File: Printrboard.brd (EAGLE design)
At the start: 100.1 x 61 mm, 122 parts, among them J1 MICROSD, J3 ATX, Q1 RFP30N06LE, Q2 RFP30N06LE, Q3 RFP30N06LE, U1 LM2841, U2 A4982, U3 A4982, U4 A4982, U5 A4982, U6 AT90USB1286, U7 AP7313, U8 TXB0104, X1 16MHz, X2 USB-MICROB

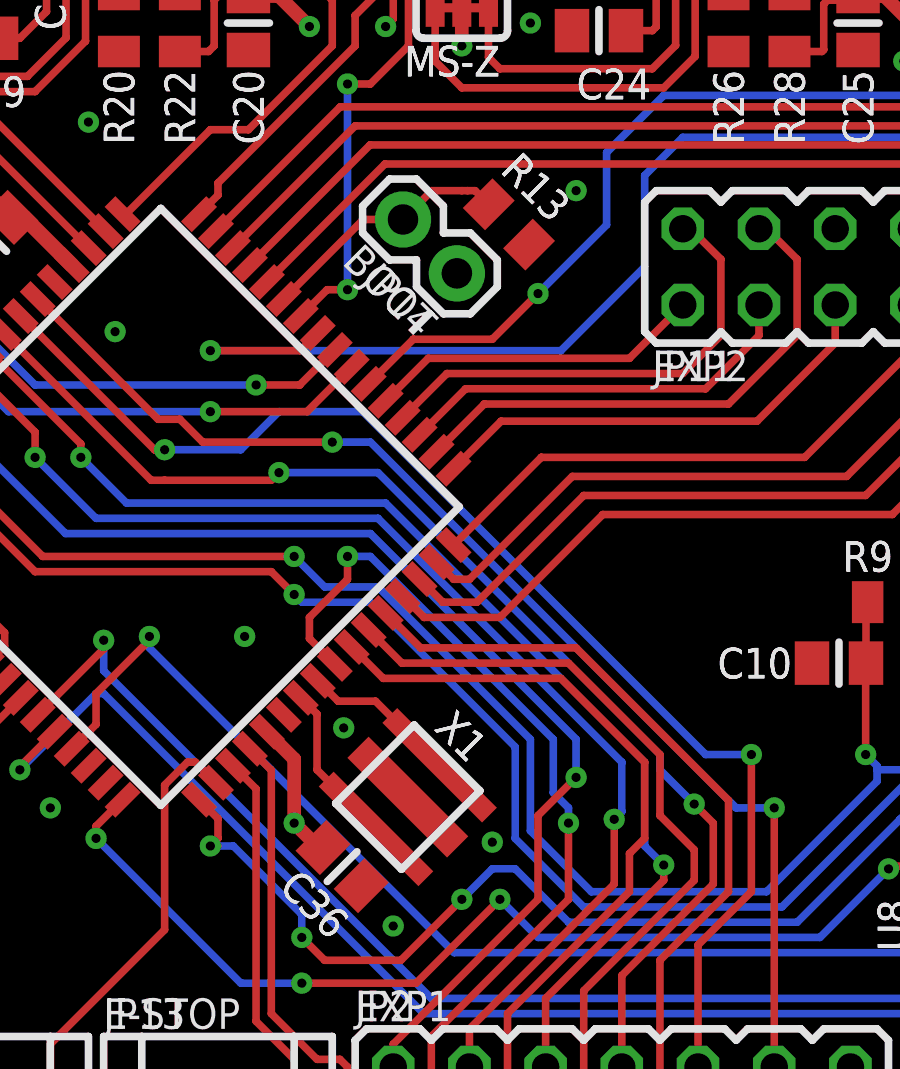
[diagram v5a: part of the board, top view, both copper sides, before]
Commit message: Make resonator pad larger to accomodate both available pacakages, and change polarity of BOOT jumper
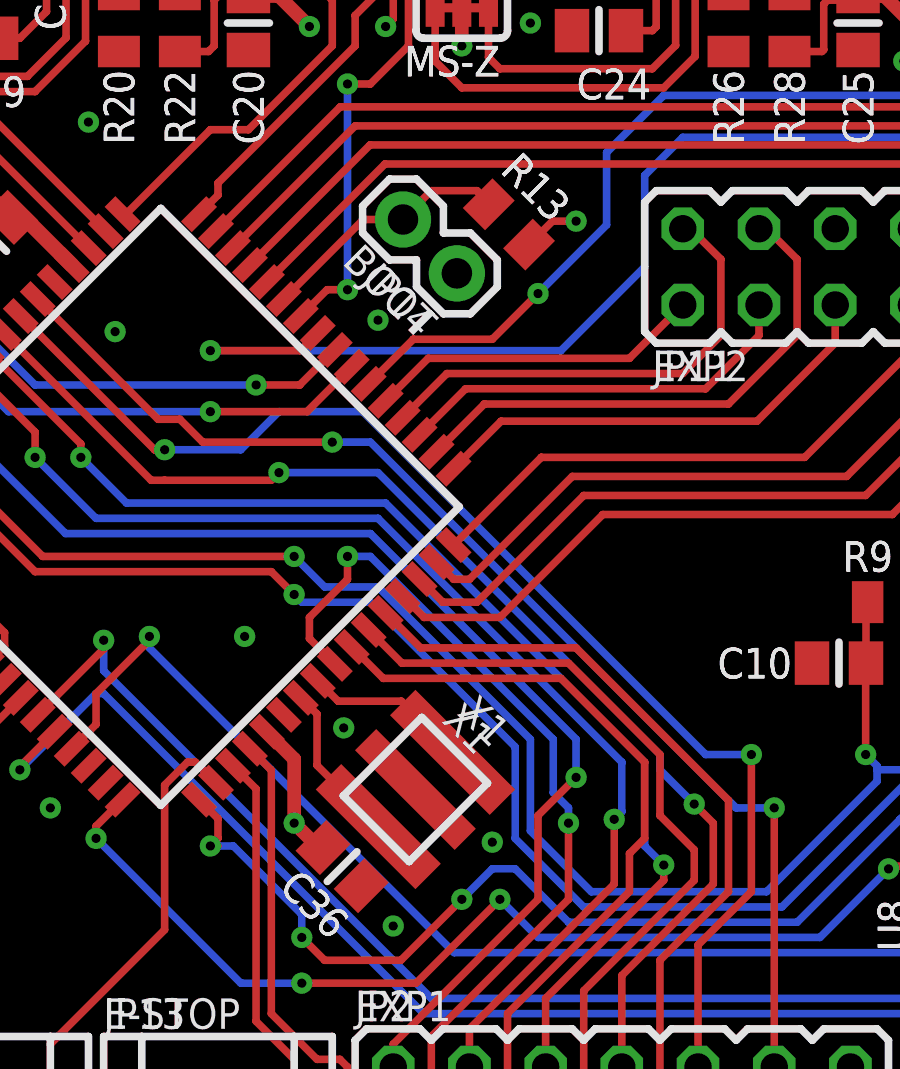
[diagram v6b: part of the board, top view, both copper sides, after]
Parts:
- JP14: value ALE -> BOOT
- moved X1 0.36 mm to (52.6, 14.1)
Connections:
- net +5V: now also R13.2; no longer JP14.1
- net GND: now also JP14.1; no longer R13.2
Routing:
- net +5V: track 151.9 -> 153.7 mm, vias 22 -> 23
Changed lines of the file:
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@@
 <layers>
 <layer number="1" name="Top" color="4" fill="1" visible="yes" active="yes"/>
-<layer number="2" name="PWR" color="16" fill="1" visible="yes" active="yes"/>
-<layer number="3" name="GND" color="17" fill="1" visible="yes" active="yes"/>
+<layer number="2" name="PWR" color="16" fill="1" visible="no" active="yes"/>
+<layer number="3" name="GND" color="17" fill="1" visible="no" active="yes"/>
 <layer number="4" name="Route4" color="1" fill="4" visible="no" active="no"/>
 <layer number="5" name="Route5" color="4" fill="4" visible="no" active="no"/>
@@
 <wire x1="26.199996875" y1="18.050003125" x2="24.600003125" y2="18.050003125" width="0.254" layer="121"/>
 <text x="24.892" y="17.926" size="1.016" layer="121" ratio="25" rot="R270">USBPWR</text>
-<wire x1="54.70636875" y1="14.033321875" x2="52.090065625" y2="11.417046875" width="0.254" layer="121"/>
-<wire x1="52.090065625" y1="11.417046875" x2="49.898046875" y2="13.609065625" width="0.254" layer="121"/>
-<wire x1="49.898046875" y1="13.609065625" x2="52.514321875" y2="16.22536875" width="0.254" layer="121"/>
-<wire x1="52.514321875" y1="16.22536875" x2="54.70636875" y2="14.033321875" width="0.254" layer="121"/>
-<text x="53.1479" y="16.086709375" size="1.016" layer="121" ratio="25" rot="R315">X1</text>
+<wire x1="54.96036875" y1="14.287321875" x2="52.344065625" y2="11.671046875" width="0.254" layer="121"/>
+<wire x1="52.344065625" y1="11.671046875" x2="50.152046875" y2="13.863065625" width="0.254" layer="121"/>
+<wire x1="50.152046875" y1="13.863065625" x2="52.768321875" y2="16.47936875" width="0.254" layer="121"/>
+<wire x1="52.768321875" y1="16.47936875" x2="54.96036875" y2="14.287321875" width="0.254" layer="121"/>
+<text x="53.9099" y="16.594709375" size="1.016" layer="121" ratio="25" rot="R315">X1</text>
 <wire x1="9.04600625" y1="2.774009375" x2="9.04600625" y2="4.37400625" width="0.254" layer="121"/>
 <wire x1="9.04600625" y1="4.37400625" x2="10.246003125" y2="4.37400625" width="0.254" layer="121"/>
@@
 <attribute name="VALUE" x="100.711" y="35.814" size="1.27" layer="27" rot="R90"/>
 </element>
-<element name="JP14" library="SparkFun" package="1X02" value="ALE" x="53.9379" y="31.2792" smashed="yes" rot="R135">
+<element name="JP14" library="SparkFun" package="1X02" value="BOOT" x="53.9379" y="31.2792" smashed="yes" rot="R135">
 <attribute name="NAME" x="53.3426" y="29.7961" size="1.016" layer="25" ratio="20" rot="R135"/>
 <attribute name="VALUE" x="57.0809" y="32.6262" size="1.27" layer="27" rot="R135"/>
@@
 <attribute name="VALUE" x="80.01" y="34.036" size="1.27" layer="27" rot="R270"/>
 </element>
-<element name="X1" library="printrbot" package="AWSCR" value="16MHz" x="52.3022" y="13.8212" smashed="yes" rot="R225">
-<attribute name="NAME" x="53.1479" y="16.0867" size="1.016" layer="25" ratio="20" rot="R315"/>
-<attribute name="VALUE" x="47.9888" y="13.4676" size="1.27" layer="27" rot="R315"/>
+<element name="X1" library="printrbot" package="AWSCR" value="16MHz" x="52.5562" y="14.0752" smashed="yes" rot="R225">
+<attribute name="NAME" x="53.4019" y="16.3407" size="1.016" layer="25" ratio="20" rot="R315"/>
+<attribute name="VALUE" x="48.2428" y="13.7216" size="1.27" layer="27" rot="R315"/>
 </element>
 <element name="C6" library="rcl" package="PANASONIC_D" value="100uF" x="10.922" y="54.102" smashed="yes" rot="R270">
@@
 <contactref element="JP12" pad="3"/>
 <contactref element="C13" pad="1"/>
-<contactref element="R13" pad="2"/>
 <contactref element="JP13" pad="3"/>
 <contactref element="C10" pad="1"/>
@@
 <contactref element="JP11" pad="1"/>
 <contactref element="JP4" pad="1"/>
-<via x="57.912" y="34.036" extent="1-16" drill="0.3048"/>
+<via x="51.308" y="29.718" extent="1-16" drill="0.3048"/>
 <via x="35.306" y="17.018" extent="1-16" drill="0.3048"/>
 <via x="32.893" y="32.385" extent="1-16" drill="0.3048"/>
@@
 <contactref element="X2" pad="MT5"/>
 <contactref element="X2" pad="MT6"/>
+<contactref element="JP14" pad="1"/>
 </signal>
 <signal name="!RESET">
@@
 <wire x1="48.17021875" y1="30.42464375" x2="50.820825" y2="33.07525" width="0.254" layer="1"/>
 <wire x1="50.820825" y1="33.07525" x2="52.141846875" y2="33.07525" width="0.254" layer="1"/>
-<wire x1="54.2924" y1="34.036" x2="54.102" y2="34.036" width="0.254" layer="1"/>
-<wire x1="54.102" y1="34.036" x2="53.086" y2="34.036" width="0.254" layer="1"/>
-<wire x1="52.141846875" y1="33.07525" x2="53.086" y2="34.019403125" width="0.254" layer="1"/>
-<wire x1="53.086" y1="34.019403125" x2="53.086" y2="34.036" width="0.254" layer="1"/>
-<wire x1="55.000346875" y1="33.58215" x2="54.546496875" y2="34.036" width="0.254" layer="1"/>
-<wire x1="54.546496875" y1="34.036" x2="54.2924" y2="34.036" width="0.254" layer="1"/>
+<wire x1="52.141846875" y1="33.07525" x2="52.141846875" y2="33.091846875" width="0.254" layer="1"/>
+<wire x1="52.141846875" y1="33.091846875" x2="53.086" y2="34.036" width="0.254" layer="1"/>
+<wire x1="53.086" y1="34.036" x2="54.61" y2="34.036" width="0.254" layer="1"/>
+<wire x1="54.61" y1="34.036" x2="55.118" y2="33.528" width="0.254" layer="1"/>
+<wire x1="55.118" y1="33.528" x2="55.000346875" y2="33.58215" width="0" layer="19" extent="1-1"/>
 </signal>
 <signal name="XTAL1">
 <contactref element="U6" pad="24"/>
 <contactref element="X1" pad="IN"/>
-<wire x1="49.9802" y1="17.018" x2="51.2266" y2="17.018" width="0.254" layer="1"/>
-<wire x1="53.362859375" y1="14.881859375" x2="53.362740625" y2="14.881859375" width="0.254" layer="1"/>
-<wire x1="53.362740625" y1="14.881859375" x2="51.2266" y2="17.018" width="0.254" layer="1"/>
-<wire x1="49.3015875" y1="17.696721875" x2="49.9802" y2="17.018109375" width="0.254" layer="1"/>
-<wire x1="49.9802" y1="17.018109375" x2="49.9802" y2="17.018" width="0.254" layer="1"/>
+<wire x1="53.793634375" y1="15.312634375" x2="52.08826875" y2="17.018" width="0.254" layer="1"/>
+<wire x1="52.08826875" y1="17.018" x2="49.980309375" y2="17.018" width="0.254" layer="1"/>
+<wire x1="49.3015875" y1="17.696721875" x2="49.980309375" y2="17.018" width="0.254" layer="1"/>
 </signal>
 <signal name="XTAL2">
 <contactref element="U6" pad="23"/>
 <contactref element="X1" pad="OUT"/>
-<wire x1="49.276" y1="14.732" x2="49.276" y2="16.590940625" width="0.254" layer="1"/>
-<wire x1="51.2415375" y1="12.7605375" x2="51.2415375" y2="12.7664625" width="0.254" layer="1"/>
-<wire x1="51.2415375" y1="12.7664625" x2="49.276" y2="14.732" width="0.254" layer="1"/>
 <wire x1="48.735903125" y1="17.1310375" x2="49.276" y2="16.590940625" width="0.254" layer="1"/>
+<wire x1="49.276" y1="16.590940625" x2="49.276" y2="14.880525" width="0.254" layer="1"/>
+<wire x1="51.3187625" y1="12.8377625" x2="49.276" y2="14.880525" width="0.254" layer="1"/>
 </signal>
 <signal name="PC2">
@@
 <contactref element="L1" pad="P$2"/>
 <contactref element="R12" pad="2"/>
-<contactref element="JP14" pad="1"/>
 <contactref element="R9" pad="2"/>
 <contactref element="R10" pad="2"/>
@@
 <contactref element="JP11" pad="2"/>
 <contactref element="JP4" pad="5"/>
-<wire x1="53.9379" y1="31.2792" x2="53.848" y2="31.2792" width="0.254" layer="16"/>
 <wire x1="23.84" y1="41.946" x2="23.84" y2="43.382" width="0.4572" layer="1"/>
 <wire x1="24.13" y1="41.656" x2="23.84" y2="41.946" width="0.4572" layer="1"/>
@@
 <wire x1="24.95" y1="20.516" x2="24.892" y2="20.574" width="0.3048" layer="1"/>
 <via x="24.892" y="20.574" extent="1-16" drill="0.3048"/>
+<contactref element="R13" pad="2"/>
+<wire x1="56.34385" y1="32.238646875" x2="57.125203125" y2="33.02" width="0.254" layer="1"/>
+<wire x1="57.125203125" y1="33.02" x2="57.912" y2="33.02" width="0.254" layer="1"/>
+<via x="57.912" y="33.02" extent="1-16" drill="0.3048"/>
 </signal>
 <signal name="SDDO">
@@
 </signal>
 </signals>
+<errors>
+</errors>
 </board>
 </drawing>

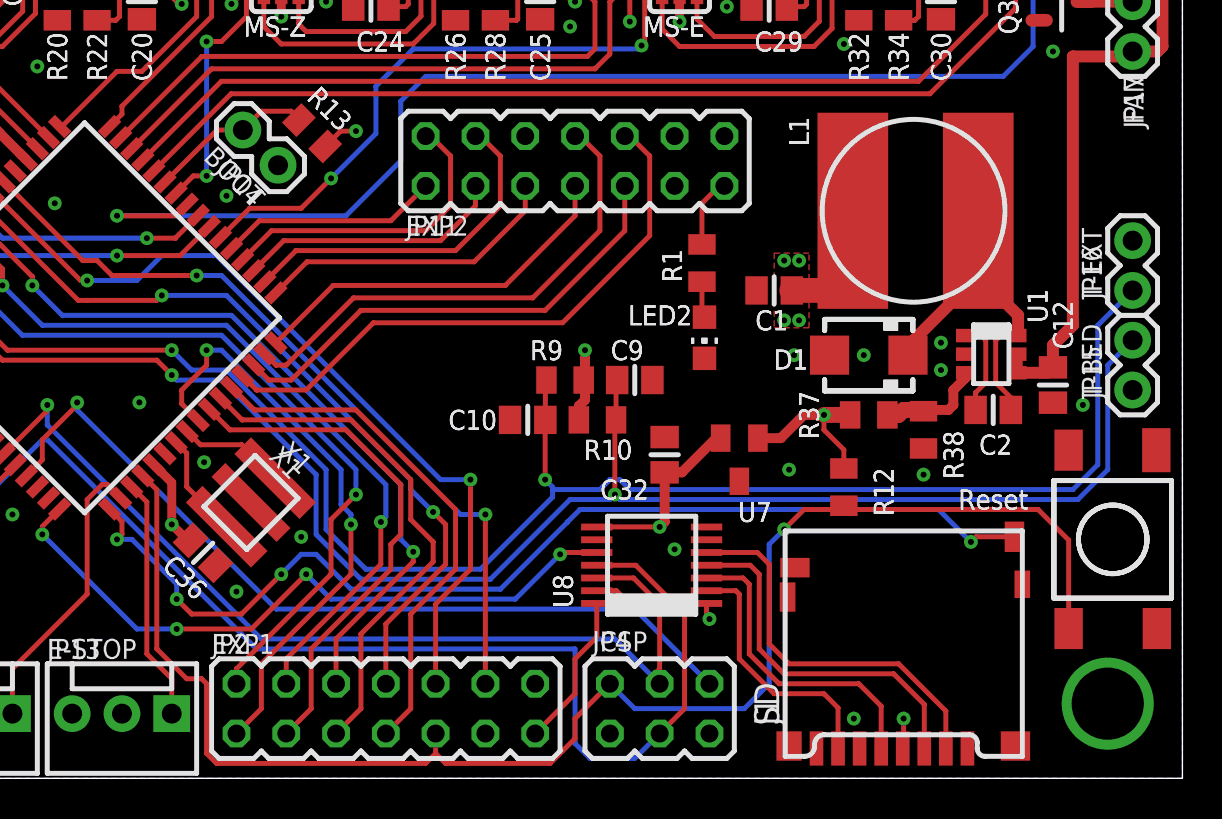
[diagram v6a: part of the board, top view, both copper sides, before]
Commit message: Small layout tweaks for Rev D
* Moved temp inputs closer to center of board and repositioned label so that
they can be seen.
* Gave the bottom expansion connector a little room by moving the ICSP port over a bit
* Moved the cap next to the resonator a little farther away from each other
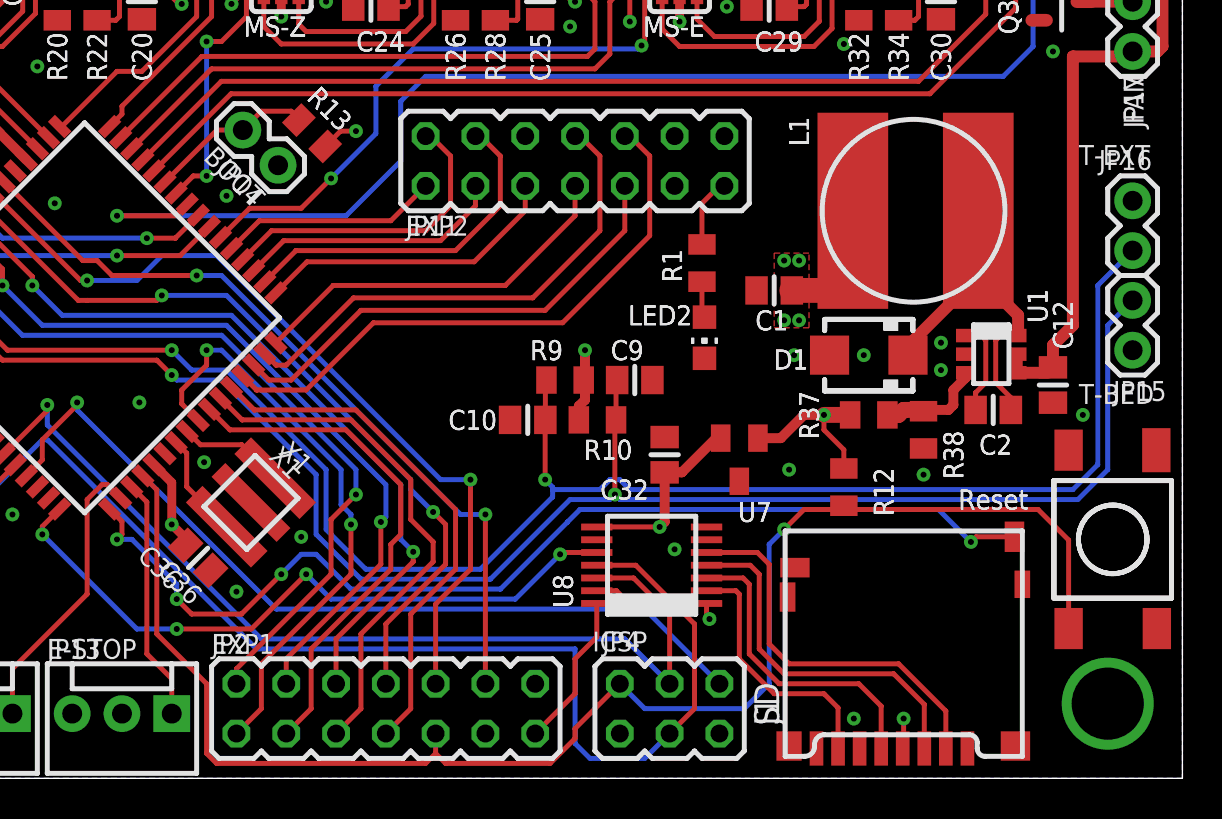
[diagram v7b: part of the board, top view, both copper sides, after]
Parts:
- moved JP15 2.03 mm to (97.5, 24.4)
- moved JP16 2.03 mm to (97.5, 26.9)
- moved JP4 0.51 mm to (73.9, 3.56)
- moved C36 0.36 mm to (49.9, 11.3)
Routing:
- net E-THERM: track 87.0 -> 89.0 mm
- net B-THERM: track 85.1 -> 87.1 mm
- net !RESET: track 78.1 -> 77.4 mm
- net MOSI: track 59.1 -> 59.8 mm
- net MISO: track 45.6 -> 46.1 mm

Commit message: Fix values for sense resistors to match BoM
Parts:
- R16, R19, R24, R25, R30, R31: value 0.1 -> 0.11
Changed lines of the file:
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@@
 <attribute name="VALUE" x="39.321" y="43.4355" size="1.27" layer="27" font="vector" ratio="10" rot="R180"/>
 </element>
-<element name="R16" library="ipc-7351-resistor" package="RESC2012X70N" value="0.1" x="45.212" y="53.594" smashed="yes">
+<element name="R16" library="ipc-7351-resistor" package="RESC2012X70N" value="0.11" x="45.212" y="53.594" smashed="yes">
 <attribute name="NAME" x="47.2455" y="55.323" size="1.016" layer="25" font="vector" ratio="20" rot="R270"/>
 <attribute name="VALUE" x="43.737" y="51.3065" size="1.27" layer="27" font="vector" ratio="10"/>
 </element>
-<element name="R19" library="ipc-7351-resistor" package="RESC2012X70N" value="0.1" x="38.608" y="53.594" smashed="yes" rot="R180">
+<element name="R19" library="ipc-7351-resistor" package="RESC2012X70N" value="0.11" x="38.608" y="53.594" smashed="yes" rot="R180">
 <attribute name="NAME" x="40.083" y="52.5765" size="1.016" layer="25" font="vector" ratio="20" rot="R180"/>
 <attribute name="VALUE" x="40.083" y="55.8815" size="1.27" layer="27" font="vector" ratio="10" rot="R180"/>
@@
 <attribute name="VALUE" x="60.149" y="43.6895" size="1.27" layer="27" font="vector" ratio="10" rot="R180"/>
 </element>
-<element name="R24" library="ipc-7351-resistor" package="RESC2012X70N" value="0.1" x="65.532" y="53.594" smashed="yes">
+<element name="R24" library="ipc-7351-resistor" package="RESC2012X70N" value="0.11" x="65.532" y="53.594" smashed="yes">
 <attribute name="NAME" x="67.5655" y="55.831" size="1.016" layer="25" font="vector" ratio="20" rot="R270"/>
 <attribute name="VALUE" x="64.057" y="51.3065" size="1.27" layer="27" font="vector" ratio="10"/>
 </element>
-<element name="R25" library="ipc-7351-resistor" package="RESC2012X70N" value="0.1" x="58.928" y="53.594" smashed="yes" rot="R180">
+<element name="R25" library="ipc-7351-resistor" package="RESC2012X70N" value="0.11" x="58.928" y="53.594" smashed="yes" rot="R180">
 <attribute name="NAME" x="60.403" y="52.5765" size="1.016" layer="25" font="vector" ratio="20" rot="R180"/>
 <attribute name="VALUE" x="60.403" y="55.8815" size="1.27" layer="27" font="vector" ratio="10" rot="R180"/>
@@
 <attribute name="VALUE" x="80.469" y="43.6895" size="1.27" layer="27" font="vector" ratio="10" rot="R180"/>
 </element>
-<element name="R30" library="ipc-7351-resistor" package="RESC2012X70N" value="0.1" x="85.852" y="53.594" smashed="yes">
+<element name="R30" library="ipc-7351-resistor" package="RESC2012X70N" value="0.11" x="85.852" y="53.594" smashed="yes">
 <attribute name="NAME" x="87.933" y="53.0875" size="1.016" layer="25" font="vector" ratio="20"/>
 <attribute name="VALUE" x="84.377" y="51.3065" size="1.27" layer="27" font="vector" ratio="10"/>
 </element>
-<element name="R31" library="ipc-7351-resistor" package="RESC2012X70N" value="0.1" x="79.248" y="53.594" smashed="yes" rot="R180">
+<element name="R31" library="ipc-7351-resistor" package="RESC2012X70N" value="0.11" x="79.248" y="53.594" smashed="yes" rot="R180">
 <attribute name="NAME" x="80.723" y="52.5765" size="1.016" layer="25" font="vector" ratio="20" rot="R180"/>
 <attribute name="VALUE" x="80.723" y="55.8815" size="1.27" layer="27" font="vector" ratio="10" rot="R180"/>
